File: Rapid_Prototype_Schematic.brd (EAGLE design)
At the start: 142 x 95 mm, 160 parts, among them IC2 SI4459ADY-T1-GE3, IC8 SI4485DY-T1-GE3, J1 XT60-M, J10 XT60-M, J2 XT60-M, J4 UJ2-MIBH-2-SMT-TR-67, J5 XT60-M, J6 XT60-M, J7 XT60-M, J8 XT60-M, J9 XT60-M, Q1 LTV-8141S, Q10 SI4435DDY, Q11 DMN65D8LFB-7, Q12 SI4435DDY, Q13 DMN65D8LFB-7, Q14 SI4435DDY, Q15 DMN65D8LFB-7, Q3 DMN65D8LFB-7, Q4 SI4435DDY, Q5 DMN65D8LFB-7, Q6 SI4435DDY, Q7 DMN65D8LFB-7, Q8 SI4435DDY, Q9 DMN65D8LFB-7, U1 LM35DM, U2 LM2904ITPX/NOPB, U3 LM2904ITPX/NOPB, U4 LM2904ITPX/NOPB, U5 LM2904ITPX/NOPB, U6 LM2904ITPX/NOPB, U7 TLV1117LV33DCYR, U8 LT1374IS8-5PBF

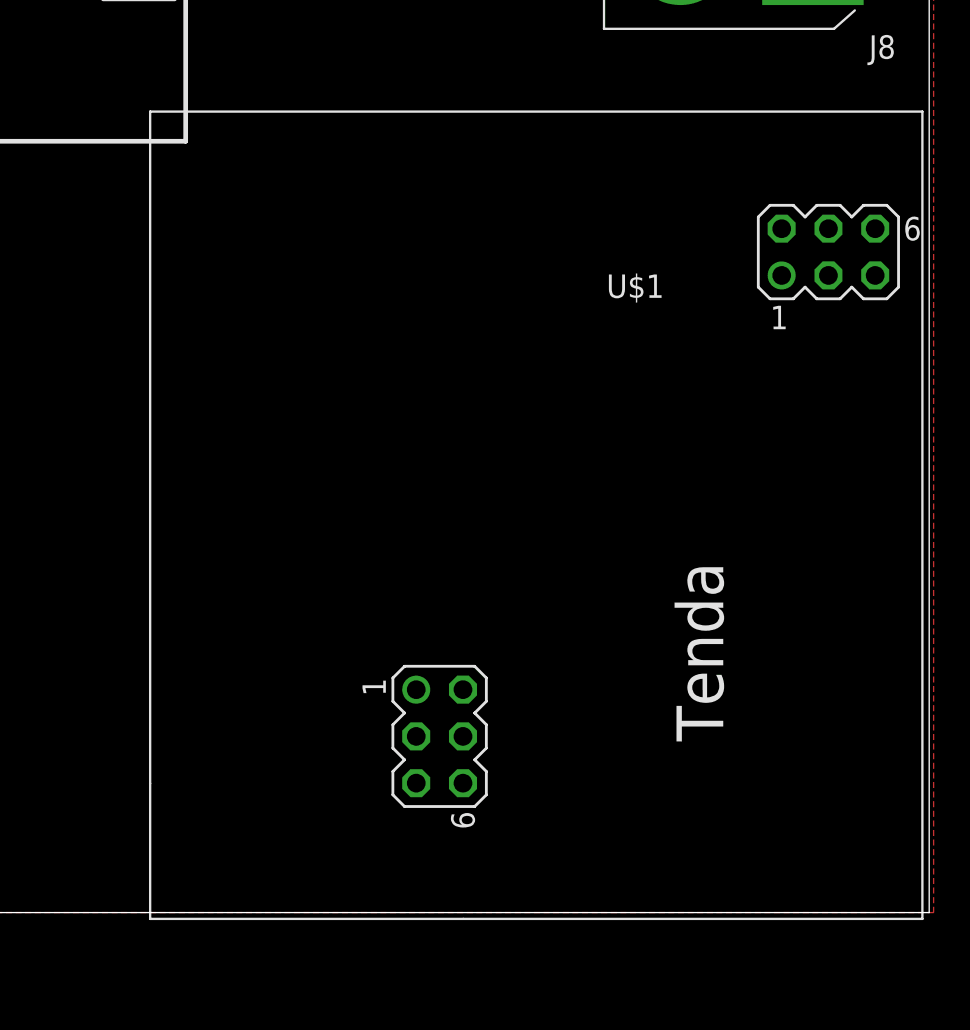
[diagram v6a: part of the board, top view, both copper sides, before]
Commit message: Changed Tenda Rotation
Changed Tenda Rotation
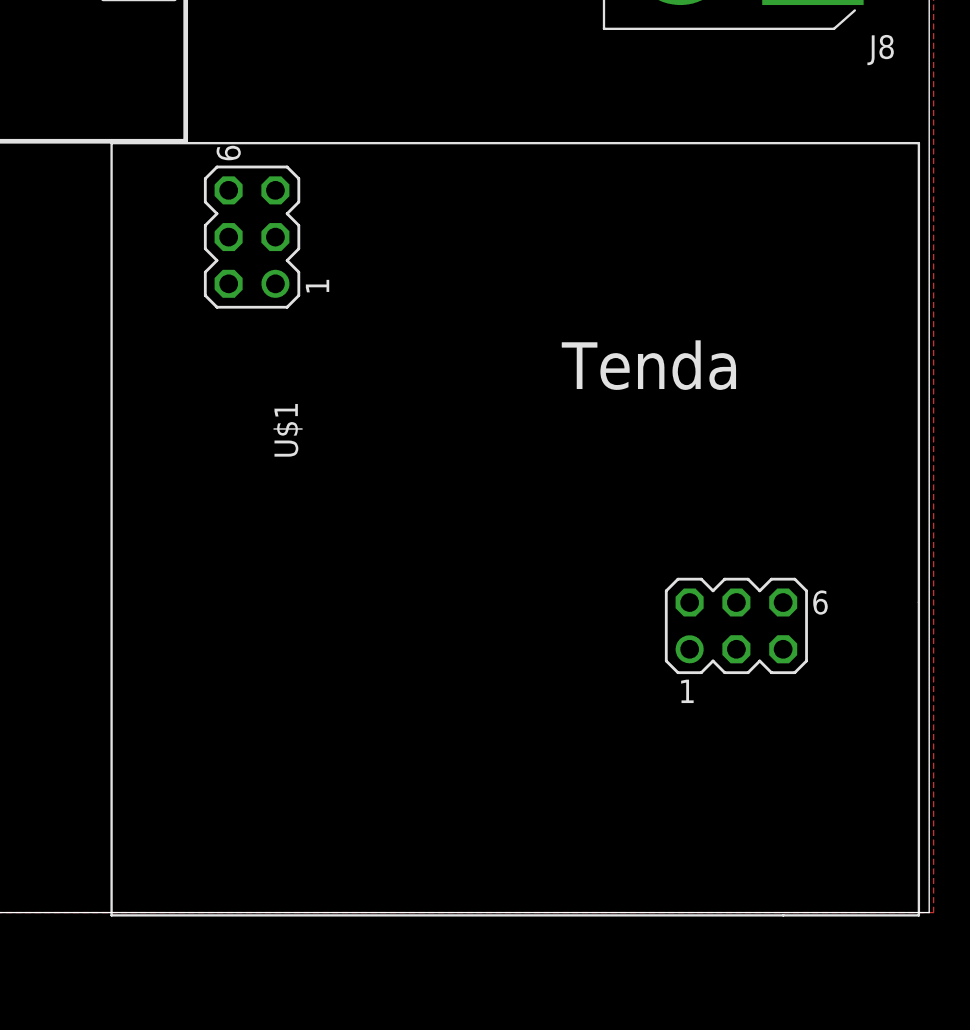
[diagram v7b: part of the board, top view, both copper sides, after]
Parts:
- moved U$1 1.37 mm to (119.5, 20.8), turned to 0 degrees
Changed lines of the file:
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@@
 <attribute name="VALUE" x="-130.81" y="-8.255" size="1.27" layer="27"/>
 </element>
-<element name="U$1" library="tenda" package="TENDA" value="TENDA" x="120.65" y="21.59" smashed="yes" rot="R270">
-<attribute name="NAME" x="118.491" y="16.51" size="1.27" layer="25" ratio="10" rot="R270"/>
-<attribute name="NAME" x="124.46" y="33.401" size="1.27" layer="25" ratio="10"/>
-<attribute name="VALUE" x="111.379" y="13.97" size="1.27" layer="27" ratio="10" rot="R270"/>
-<attribute name="VALUE" x="127" y="26.289" size="1.27" layer="27" ratio="10"/>
+<element name="U$1" library="tenda" package="TENDA" value="TENDA" x="119.507" y="20.828" smashed="yes">
+<attribute name="NAME" x="124.587" y="18.669" size="1.27" layer="25" ratio="10"/>
+<attribute name="NAME" x="107.696" y="24.638" size="1.27" layer="25" ratio="10" rot="R90"/>
+<attribute name="VALUE" x="127.127" y="11.557" size="1.27" layer="27" ratio="10"/>
+<attribute name="VALUE" x="114.808" y="27.178" size="1.27" layer="27" ratio="10" rot="R90"/>
 </element>
 </elements>
@@
 <wire x1="135.68" y1="52.07" x2="135.68" y2="60.96" width="0" layer="19" extent="1-1"/>
 <wire x1="107.53" y1="91.44" x2="135.68" y2="87.63" width="0" layer="19" extent="1-1"/>
-<wire x1="114.128296875" y1="12.11275" x2="135.68" y2="52.07" width="0" layer="19" extent="1-1"/>
+<wire x1="128.98425" y1="14.306296875" x2="135.68" y2="52.07" width="0" layer="19" extent="1-1"/>
 <wire x1="60.96" y1="92.71" x2="107.53" y2="91.44" width="0" layer="19" extent="1-1"/>
 <wire x1="58.42" y1="92.71" x2="60.96" y2="92.71" width="0" layer="19" extent="1-1"/>
@@
 <contactref element="U$1" pad="11"/>
 <contactref element="U$1" pad="12"/>
-<wire x1="114.128296875" y1="7.03275" x2="116.668296875" y2="7.03275" width="0" layer="19" extent="1-1"/>
-<wire x1="-27.94" y1="87.05215" x2="114.128296875" y2="7.03275" width="0" layer="19" extent="1-1"/>
+<wire x1="134.06425" y1="14.306296875" x2="134.06425" y2="16.846296875" width="0" layer="19" extent="1-1"/>
+<wire x1="-27.94" y1="87.05215" x2="134.06425" y2="14.306296875" width="0" layer="19" extent="1-1"/>
 <wire x1="-27.94" y1="93.28785" x2="-27.94" y2="87.05215" width="0" layer="19" extent="1-1"/>
 <wire x1="-59.27" y1="113.03" x2="-27.94" y2="93.28785" width="0" layer="19" extent="1-1"/>
@@
 <contactref element="R3" pad="1"/>
 <contactref element="U$1" pad="10"/>
-<wire x1="-130.54" y1="113.03" x2="116.668296875" y2="9.57275" width="0" layer="19" extent="1-1"/>
+<wire x1="-130.54" y1="113.03" x2="131.52425" y2="16.846296875" width="0" layer="19" extent="1-1"/>
 </signal>
 <signal name="N$54">
@@
 <contactref element="R5" pad="1"/>
 <contactref element="U$1" pad="8"/>
-<wire x1="-17.51" y1="119.38" x2="116.668296875" y2="12.11275" width="0" layer="19" extent="1-1"/>
+<wire x1="-17.51" y1="119.38" x2="128.98425" y2="16.846296875" width="0" layer="19" extent="1-1"/>
 </signal>
 <signal name="N$56">
@@
 <contactref element="R6" pad="1"/>
 <contactref element="U$1" pad="9"/>
-<wire x1="-22.59" y1="119.38" x2="114.128296875" y2="9.57275" width="0" layer="19" extent="1-1"/>
+<wire x1="-22.59" y1="119.38" x2="131.52425" y2="14.306296875" width="0" layer="19" extent="1-1"/>
 </signal>
 <signal name="N$58">
@@
 <contactref element="U$1" pad="5"/>
 <contactref element="U$1" pad="6"/>
-<wire x1="139.065" y1="34.6202" x2="139.065" y2="37.1602" width="0" layer="19" extent="1-1"/>
-<wire x1="-93.45" y1="104.14" x2="139.065" y2="37.1602" width="0" layer="19" extent="1-1"/>
+<wire x1="106.4768" y1="39.243" x2="103.9368" y2="39.243" width="0" layer="19" extent="1-1"/>
+<wire x1="-93.45" y1="104.14" x2="103.9368" y2="39.243" width="0" layer="19" extent="1-1"/>
 <wire x1="-131.23" y1="132.08" x2="-93.45" y2="104.14" width="0" layer="19" extent="1-1"/>
 <wire x1="-127" y1="-5.08" x2="-93.45" y2="104.14" width="0" layer="19" extent="1-1"/>
@@
 <contactref element="U$1" pad="1"/>
 <contactref element="U$1" pad="2"/>
-<wire x1="133.985" y1="34.6202" x2="133.985" y2="37.1602" width="0" layer="19" extent="1-1"/>
-<wire x1="-129.54" y1="-5.08" x2="133.985" y2="34.6202" width="0" layer="19" extent="1-1"/>
+<wire x1="106.4768" y1="34.163" x2="103.9368" y2="34.163" width="0" layer="19" extent="1-1"/>
+<wire x1="-129.54" y1="-5.08" x2="106.4768" y2="34.163" width="0" layer="19" extent="1-1"/>
 </signal>
 <signal name="ESCSF_POWER">

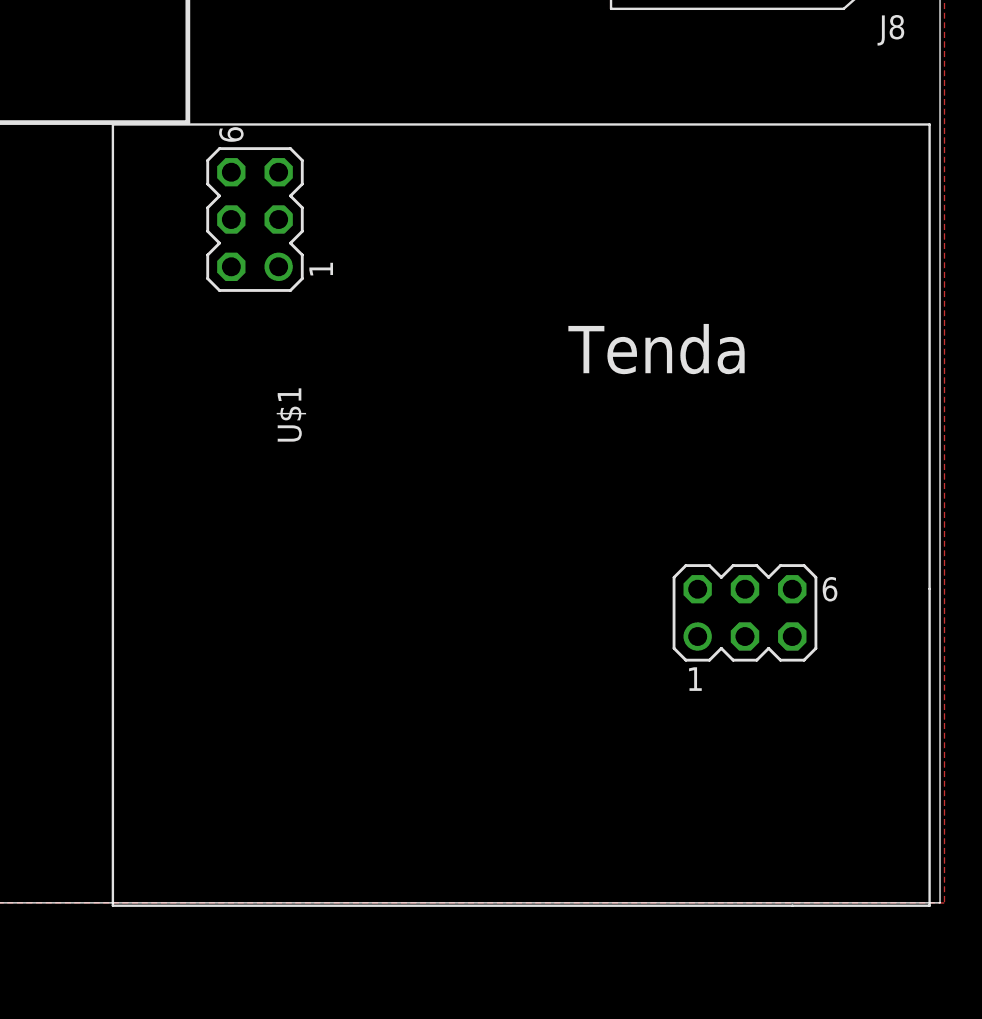
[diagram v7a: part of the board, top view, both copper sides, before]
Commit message: Update Rapid_Prototype_Schematic.brd
Minor Tenda Position Adjustment
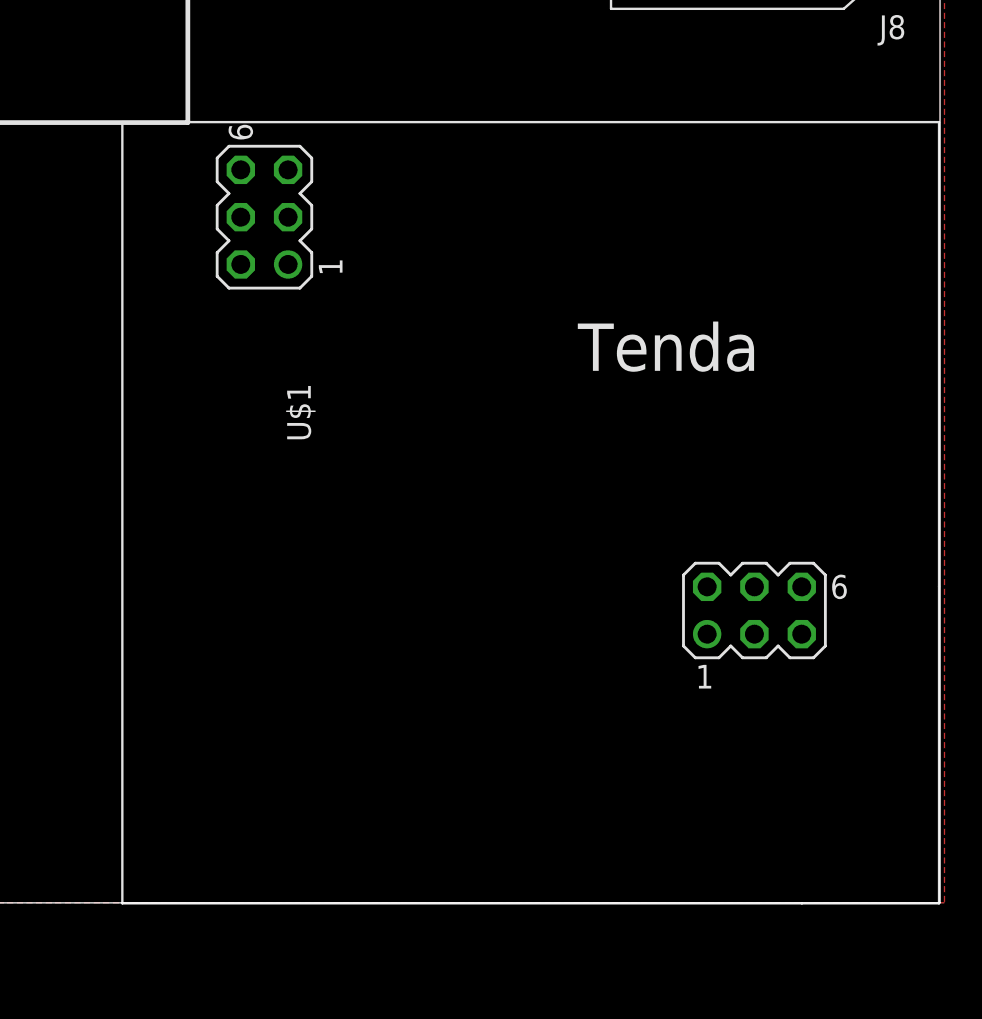
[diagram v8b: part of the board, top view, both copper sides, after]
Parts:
- moved U$1 0.52 mm to (120.0, 21.0)
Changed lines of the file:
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@@
 <attribute name="VALUE" x="-130.81" y="-8.255" size="1.27" layer="27"/>
 </element>
-<element name="U$1" library="tenda" package="TENDA" value="TENDA" x="119.507" y="20.828" smashed="yes">
-<attribute name="NAME" x="124.587" y="18.669" size="1.27" layer="25" ratio="10"/>
-<attribute name="NAME" x="107.696" y="24.638" size="1.27" layer="25" ratio="10" rot="R90"/>
-<attribute name="VALUE" x="127.127" y="11.557" size="1.27" layer="27" ratio="10"/>
-<attribute name="VALUE" x="114.808" y="27.178" size="1.27" layer="27" ratio="10" rot="R90"/>
+<element name="U$1" library="tenda" package="TENDA" value="TENDA" x="120.015" y="20.955" smashed="yes">
+<attribute name="NAME" x="125.095" y="18.796" size="1.27" layer="25" ratio="10"/>
+<attribute name="NAME" x="108.204" y="24.765" size="1.27" layer="25" ratio="10" rot="R90"/>
+<attribute name="VALUE" x="127.635" y="11.684" size="1.27" layer="27" ratio="10"/>
+<attribute name="VALUE" x="115.316" y="27.305" size="1.27" layer="27" ratio="10" rot="R90"/>
 </element>
 </elements>
@@
 <wire x1="135.68" y1="52.07" x2="135.68" y2="60.96" width="0" layer="19" extent="1-1"/>
 <wire x1="107.53" y1="91.44" x2="135.68" y2="87.63" width="0" layer="19" extent="1-1"/>
-<wire x1="128.98425" y1="14.306296875" x2="135.68" y2="52.07" width="0" layer="19" extent="1-1"/>
+<wire x1="129.49225" y1="14.433296875" x2="135.68" y2="52.07" width="0" layer="19" extent="1-1"/>
 <wire x1="60.96" y1="92.71" x2="107.53" y2="91.44" width="0" layer="19" extent="1-1"/>
 <wire x1="58.42" y1="92.71" x2="60.96" y2="92.71" width="0" layer="19" extent="1-1"/>
@@
 <contactref element="U$1" pad="11"/>
 <contactref element="U$1" pad="12"/>
-<wire x1="134.06425" y1="14.306296875" x2="134.06425" y2="16.846296875" width="0" layer="19" extent="1-1"/>
-<wire x1="-27.94" y1="87.05215" x2="134.06425" y2="14.306296875" width="0" layer="19" extent="1-1"/>
+<wire x1="134.57225" y1="14.433296875" x2="134.57225" y2="16.973296875" width="0" layer="19" extent="1-1"/>
+<wire x1="-27.94" y1="87.05215" x2="134.57225" y2="14.433296875" width="0" layer="19" extent="1-1"/>
 <wire x1="-27.94" y1="93.28785" x2="-27.94" y2="87.05215" width="0" layer="19" extent="1-1"/>
 <wire x1="-59.27" y1="113.03" x2="-27.94" y2="93.28785" width="0" layer="19" extent="1-1"/>
@@
 <contactref element="R3" pad="1"/>
 <contactref element="U$1" pad="10"/>
-<wire x1="-130.54" y1="113.03" x2="131.52425" y2="16.846296875" width="0" layer="19" extent="1-1"/>
+<wire x1="-130.54" y1="113.03" x2="132.03225" y2="16.973296875" width="0" layer="19" extent="1-1"/>
 </signal>
 <signal name="N$54">
@@
 <contactref element="R5" pad="1"/>
 <contactref element="U$1" pad="8"/>
-<wire x1="-17.51" y1="119.38" x2="128.98425" y2="16.846296875" width="0" layer="19" extent="1-1"/>
+<wire x1="-17.51" y1="119.38" x2="129.49225" y2="16.973296875" width="0" layer="19" extent="1-1"/>
 </signal>
 <signal name="N$56">
@@
 <contactref element="R6" pad="1"/>
 <contactref element="U$1" pad="9"/>
-<wire x1="-22.59" y1="119.38" x2="131.52425" y2="14.306296875" width="0" layer="19" extent="1-1"/>
+<wire x1="-22.59" y1="119.38" x2="132.03225" y2="14.433296875" width="0" layer="19" extent="1-1"/>
 </signal>
 <signal name="N$58">
@@
 <contactref element="U$1" pad="5"/>
 <contactref element="U$1" pad="6"/>
-<wire x1="106.4768" y1="39.243" x2="103.9368" y2="39.243" width="0" layer="19" extent="1-1"/>
-<wire x1="-93.45" y1="104.14" x2="103.9368" y2="39.243" width="0" layer="19" extent="1-1"/>
+<wire x1="106.9848" y1="39.37" x2="104.4448" y2="39.37" width="0" layer="19" extent="1-1"/>
+<wire x1="-93.45" y1="104.14" x2="104.4448" y2="39.37" width="0" layer="19" extent="1-1"/>
 <wire x1="-131.23" y1="132.08" x2="-93.45" y2="104.14" width="0" layer="19" extent="1-1"/>
 <wire x1="-127" y1="-5.08" x2="-93.45" y2="104.14" width="0" layer="19" extent="1-1"/>
@@
 <contactref element="U$1" pad="1"/>
 <contactref element="U$1" pad="2"/>
-<wire x1="106.4768" y1="34.163" x2="103.9368" y2="34.163" width="0" layer="19" extent="1-1"/>
-<wire x1="-129.54" y1="-5.08" x2="106.4768" y2="34.163" width="0" layer="19" extent="1-1"/>
+<wire x1="106.9848" y1="34.29" x2="104.4448" y2="34.29" width="0" layer="19" extent="1-1"/>
+<wire x1="-129.54" y1="-5.08" x2="106.9848" y2="34.29" width="0" layer="19" extent="1-1"/>
 </signal>
 <signal name="ESCSF_POWER">
